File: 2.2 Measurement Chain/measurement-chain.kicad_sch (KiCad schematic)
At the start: 22 parts, among them J1 M12 5-Pin Socket, U1 TLV9062xD, U2 TLV9062xD, U3 ADS1251, U4 AZ1117-ADJ

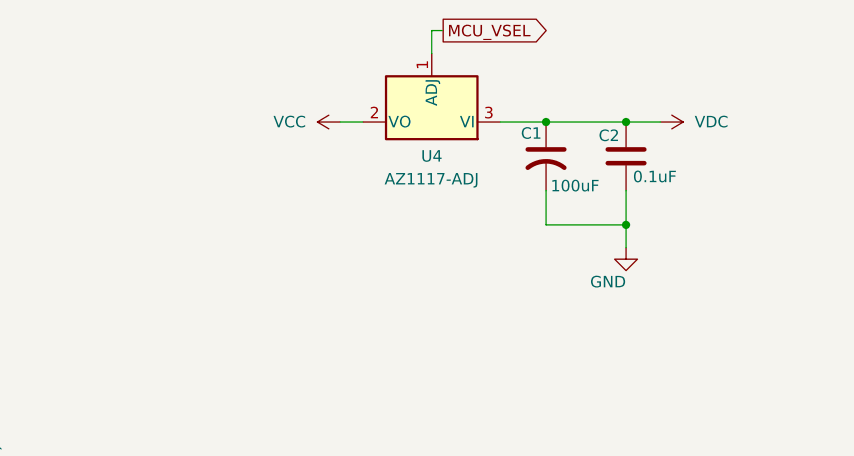
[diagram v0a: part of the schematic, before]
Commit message: minor updates to schematic
just added more decoupling caps
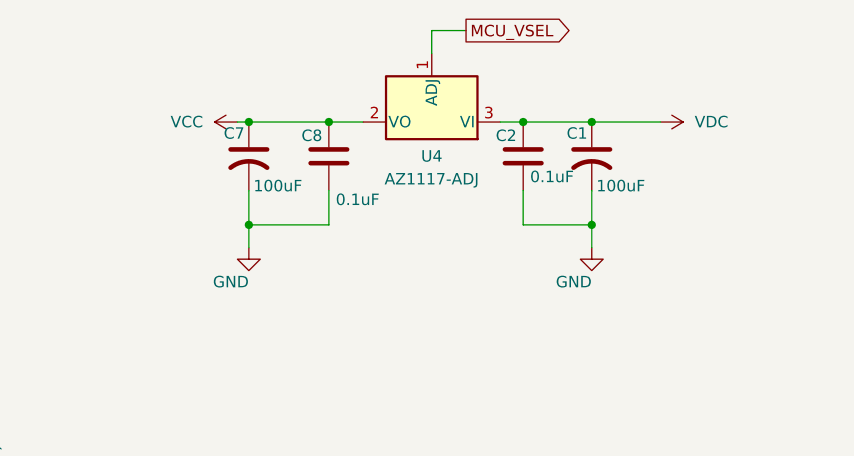
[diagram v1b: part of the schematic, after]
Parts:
- added C7: 100uF, symbol Device:C_US
- added C8: 0.1uF, symbol Device:C
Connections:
- net GND: now also C7.2, C8.2
- net VCC: now also C7.1, C8.1
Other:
- moved on the sheet: C1, C2
